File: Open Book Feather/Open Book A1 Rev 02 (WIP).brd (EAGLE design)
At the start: 77.5 x 112.3 mm, 114 parts, among them J1 SJ-43514-SMT, J2 10118193-0001LF, Q1 DMG341, Q2 IRLML0100, SW1 SPDT_SWITCH, U1 AP2112-3.3, U2 MCP73831T-2ACI/OT, U3 ATSAMD51J64-TQFP(10X10), U4 GD25Q16C (or GD25Q32C), U5 74AC165D, U6 GD25Q16C (or GD25Q32C), U7 23K256-I/SN, X1 JSTPH, X2 2x5 0.05" SWD

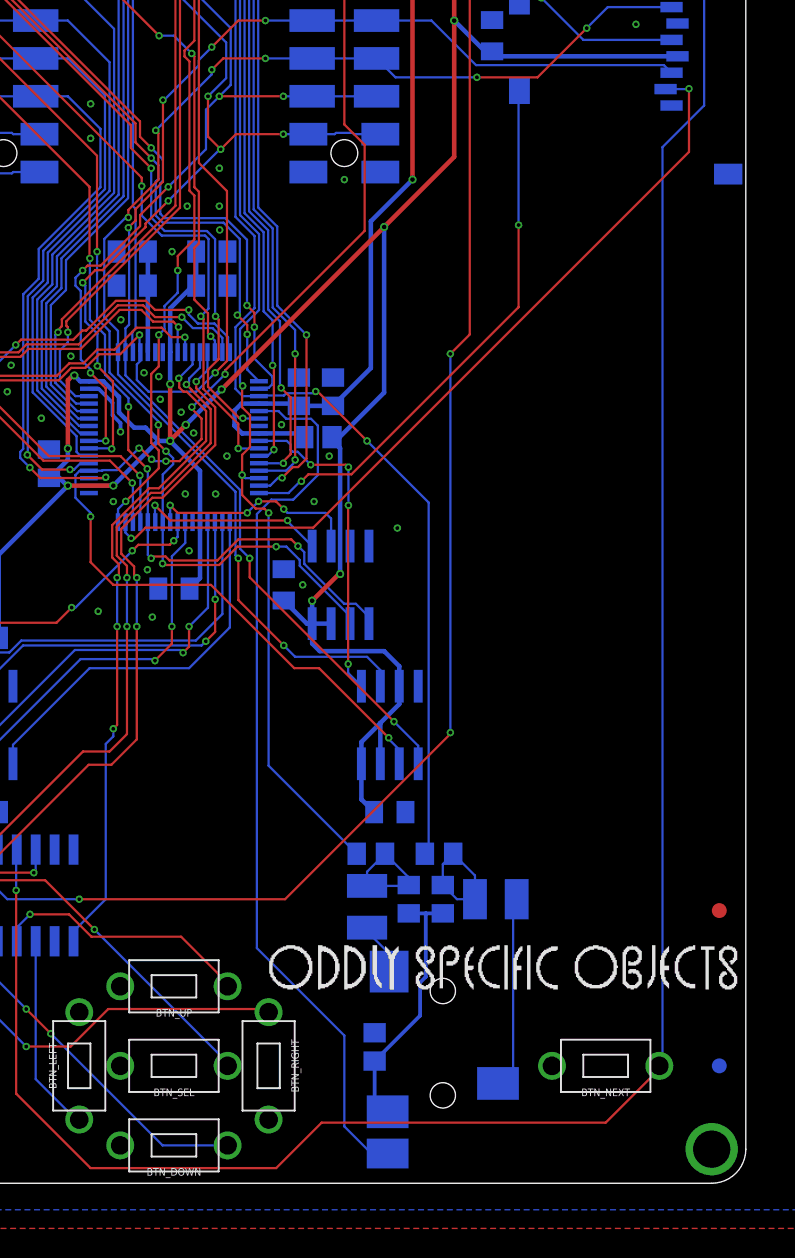
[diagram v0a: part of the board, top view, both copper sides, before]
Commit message: added mic preamp
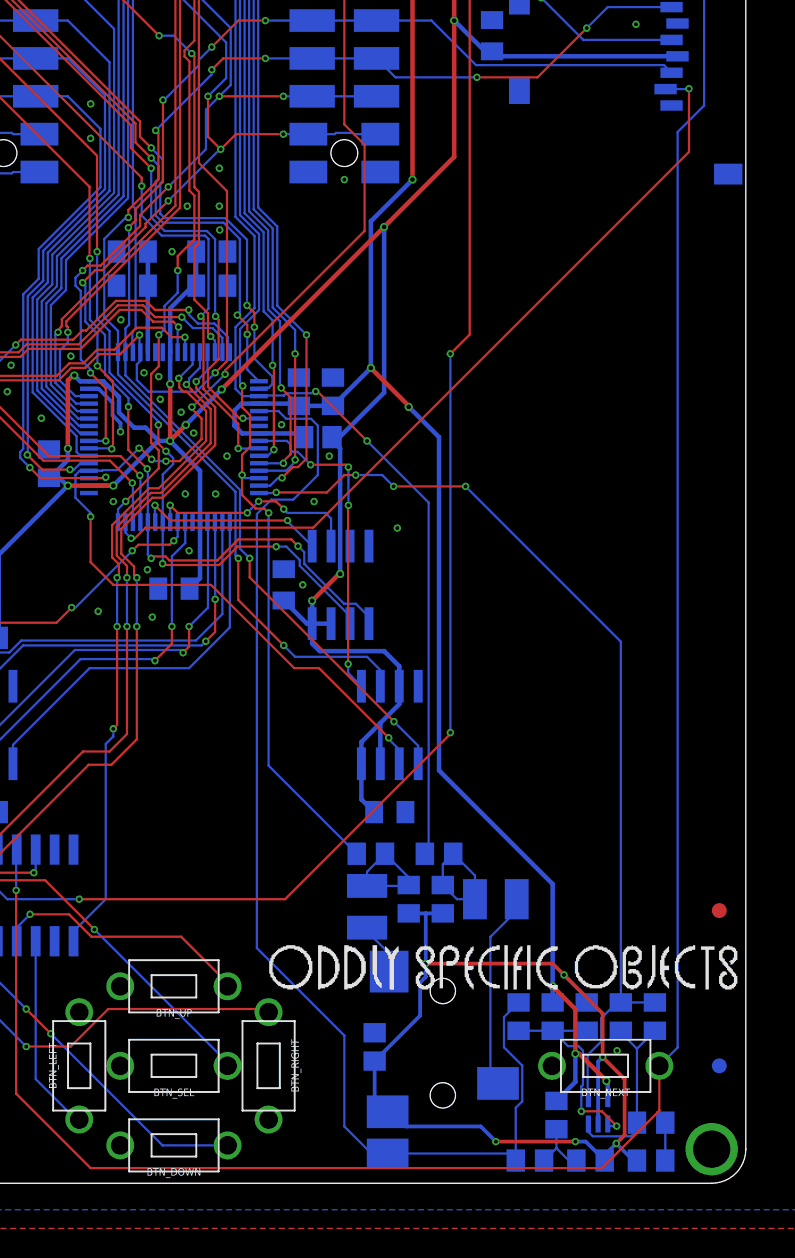
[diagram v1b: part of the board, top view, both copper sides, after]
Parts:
- added C32: 0.1µF, microbuilder:0805-NO
- added C33: 0.01uF, microbuilder:0805-NO
- added C34: 100pF, microbuilder:0805-NO
- added C35: 10uF, microbuilder:0805-NO
- added R10, R11: 1M, microbuilder:0805-NO
- added R12: 100K, microbuilder:0805-NO
- added R13, R23, R24: 1K, microbuilder:0805-NO
- added U8: MAX4466EXK+T, microbuilder:SC70-5
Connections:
- new net A10_MICAMP: C34.1, R12.2, U3.16, U8.4
- new net N$65: C32.1, R13.2, R23.1
- new net N$67: C33.2, R10.2, R11.1, U8.1
- new net N$68: C34.2, R12.1, R24.1, U8.3
- new net N$69: C35.1, R24.2
- net A7_MIC: now also C33.1, R13.1
- net AGND: now also C32.2, C35.2, R10.1, U8.2
- net AVCC: now also R11.2, R23.2, U8.5
- net SD_CD: no longer U3.16
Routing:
- net A10_MICAMP: track 0.00 -> 63.4 mm, vias 0 -> 4
- net AVCC: track 69.3 -> 129.8 mm, vias 2 -> 7
- net AGND: track 17.4 -> 66.5 mm, vias 0 -> 6
- net SD_CD: track 37.1 -> 0.00 mm, vias 2 -> 0
- net A7_MIC: track 60.0 -> 80.5 mm
- net N$67: track 0.00 -> 14.7 mm, vias 0 -> 2
- net N$68: track 0.00 -> 12.9 mm
- net N$65: track 0.00 -> 4.12 mm
- net N$69: track 0.00 -> 2.54 mm
- net BUTTON6: track 147.7 -> 149.3 mm
- net GND: vias 44 -> 45
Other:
- board text added: "+MIC PREAMP"
- board text added: "A0: Right audio out A1: Left audio out A7: Raw mic in"
- board text added: "U8 is a MAX4466 amp for an inline electret mic. A10: louder mic in."
- board text removed: "(like the old iPhone ones) you can detect button presses when A7 shorts to ground."
- board text removed: "3.5mm jack J1 does a lot! Dual DACs on A0 and A1 drive the R and L channels, respectively. If your earphones have an inline mic, you can read that signal on pin A7. And if it has a one button remote"

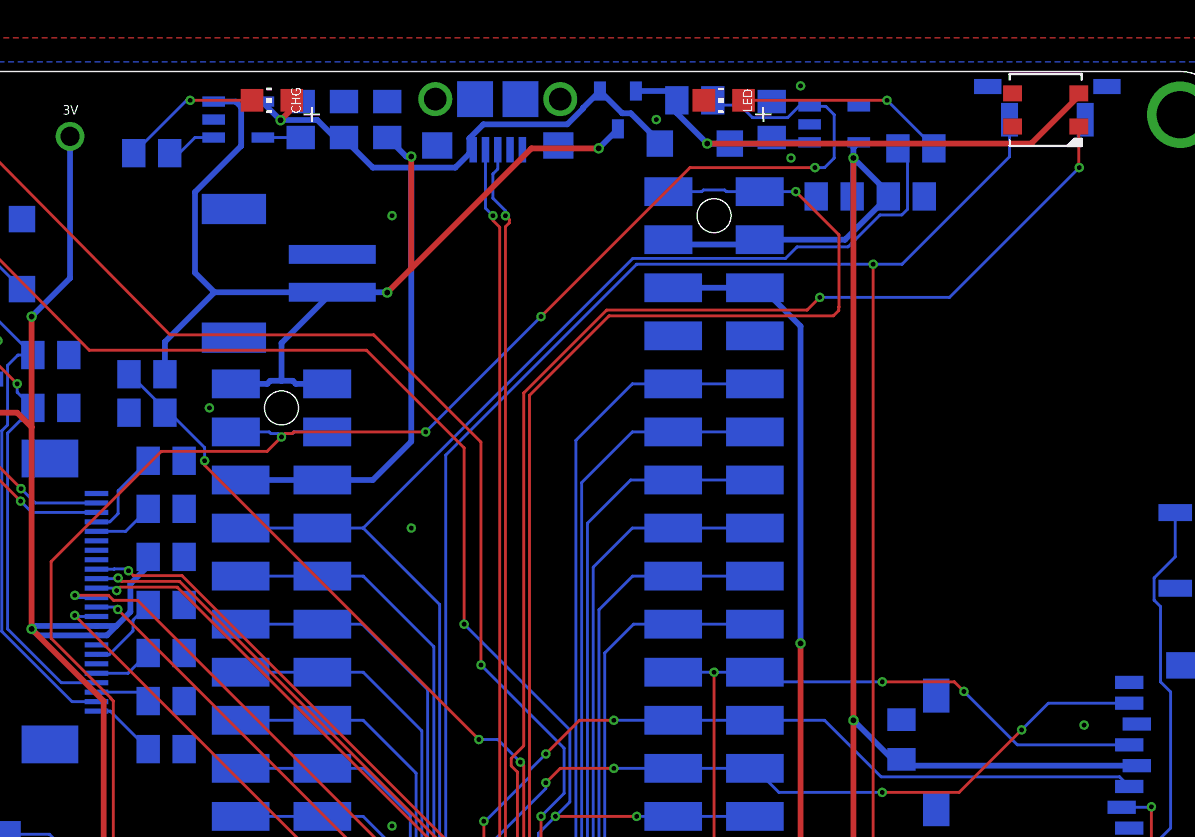
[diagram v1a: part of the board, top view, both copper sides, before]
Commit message: rearrange power supply block, power neopixel from regulator
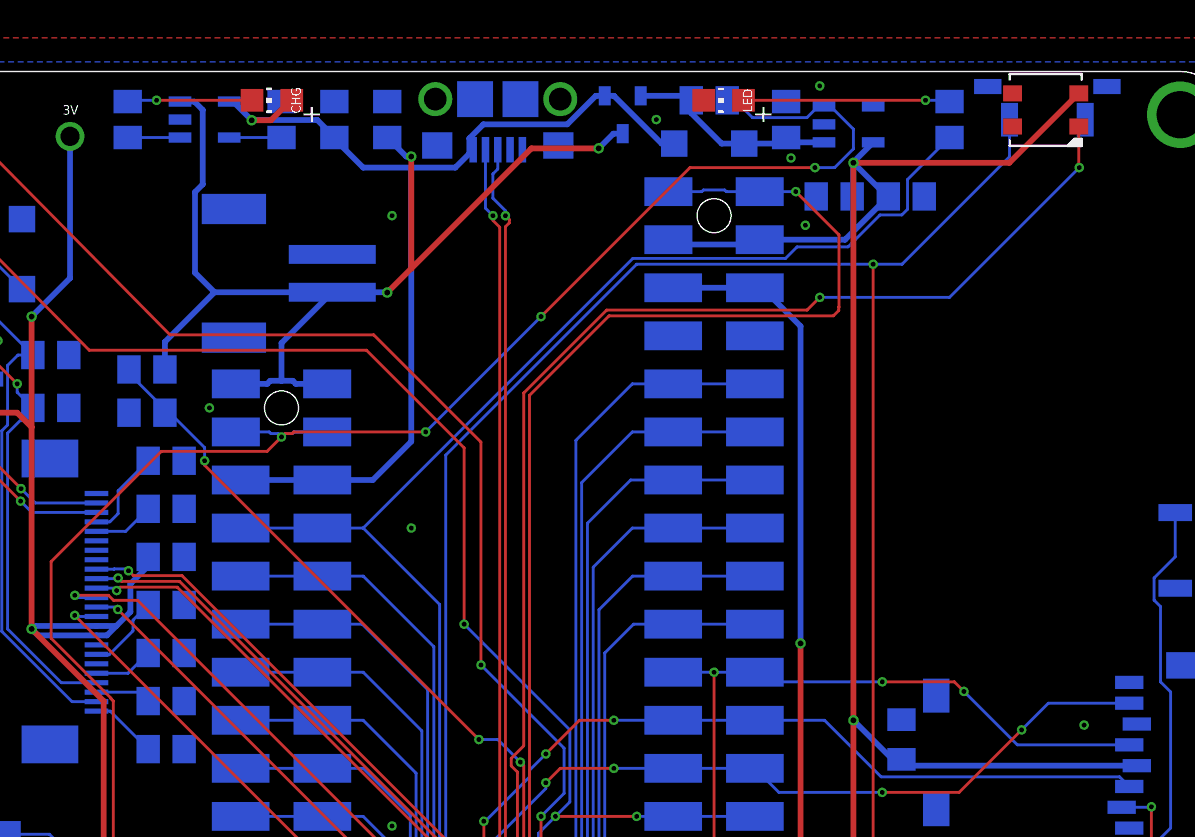
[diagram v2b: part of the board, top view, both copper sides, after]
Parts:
- moved R8 2.34 mm to (62.7, 109.7), turned to 90 degrees
- moved R4 2.18 mm to (19.3, 109.7), turned to 270 degrees
- moved U2 1.78 mm to (23.4, 109.7)
- moved R3 1.02 mm to (27.4, 109.7)
- moved U1 0.76 mm to (57.4, 109.5)
- moved C1 0.76 mm to (54.1, 109.7)
- moved D1 0.76 mm to (50.0, 108.5)
- moved R1 0.76 mm to (50.0, 110.7)
- moved R2 0.51 mm to (30.2, 109.7)
- moved Q1 0.36 mm to (45.5, 110.0)
- moved R15 0.25 mm to (20.3, 96.5)
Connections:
- net +3V3: now also STATUS.2
- net V+: no longer STATUS.2
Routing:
- net V+: track 31.8 -> 11.4 mm, vias 1 -> 0
- net +3V3: track 434.0 -> 447.3 mm
- net VBUS: track 51.8 -> 55.3 mm
- net VBAT: track 61.5 -> 60.2 mm
- net D13: track 87.3 -> 88.6 mm
- net N$4: track 7.41 -> 6.60 mm
- net PROG: track 2.00 -> 2.76 mm
- net EN: track 152.0 -> 152.6 mm
- net GND: vias 45 -> 46
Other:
- board text added: "(for red LED #13)"

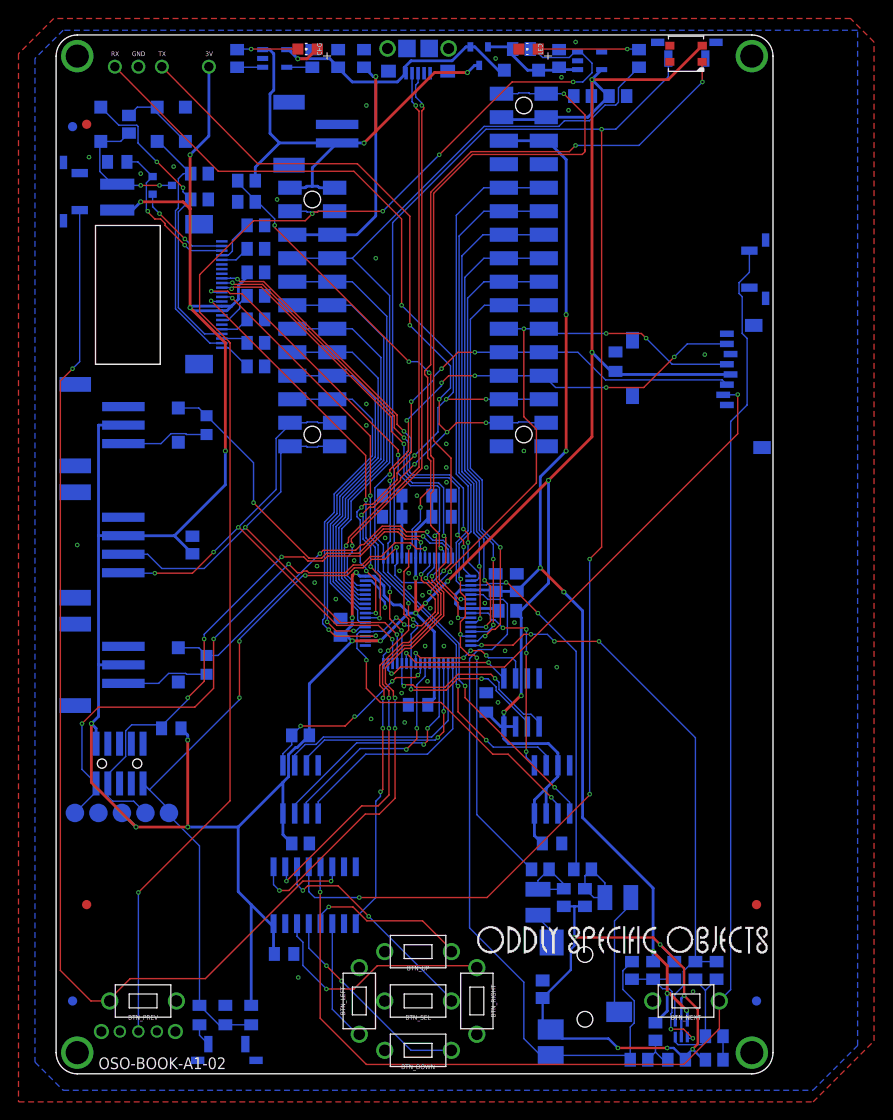
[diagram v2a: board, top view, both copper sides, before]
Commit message: fix buttons, add pulldown resistors & remove lock btn from shift reg
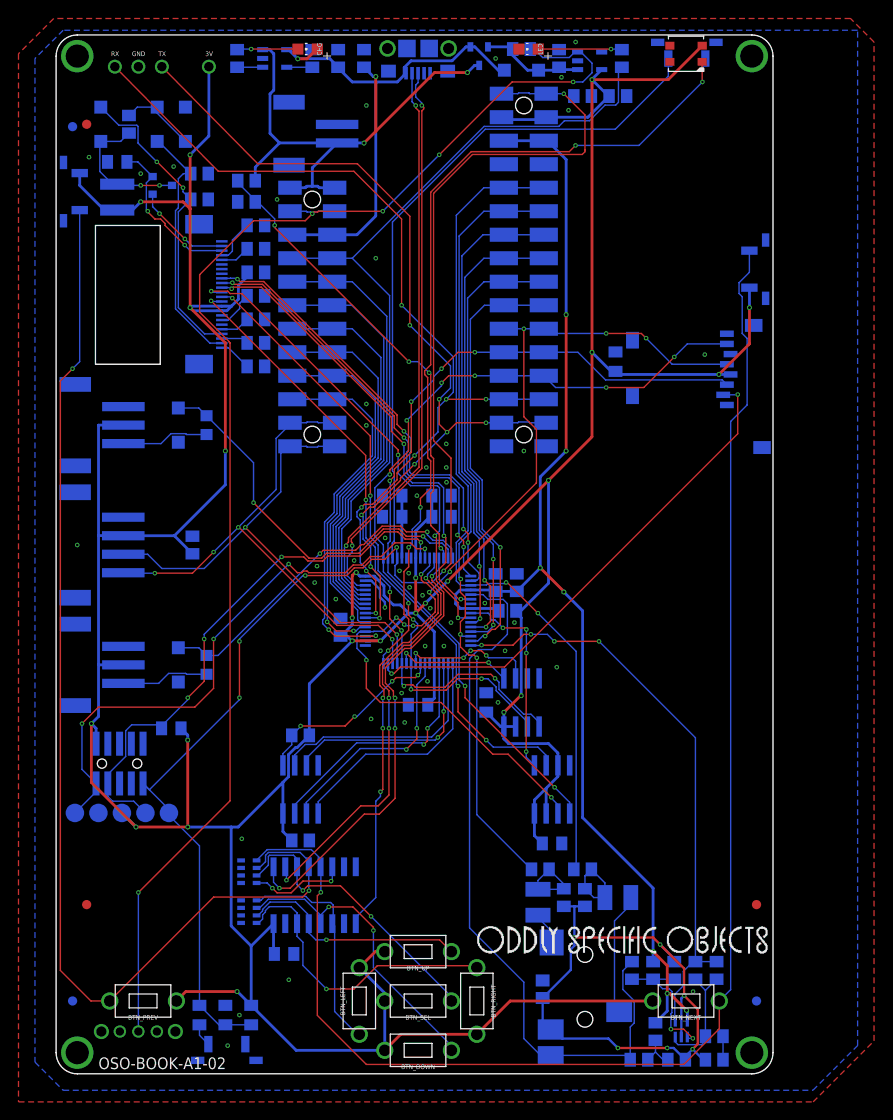
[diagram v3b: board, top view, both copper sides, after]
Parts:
- added R26, R27: 100K, resistor array:EXBV8V
- LED: value RED OR GRN -> RED
- moved R8 1.85 mm to (60.9, 109.7)
- moved C14 0.33 mm to (26.2, 25.2)
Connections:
- new net BUTTONLOCK: BTN_LOCK.P$1, U3.51
- net +3V3: now also BTN_NEXT_ALT.P$2, BTN_PREV_ALT.P$2, U$23.P$2, U$46.P$2, U$49.P$2, U$50.P$2, U$51.P$2, U$52.P$2, U$53.P$2
- net BUTTON0: now also R27.1
- net BUTTON1: now also R27.2, U$23.P$1; no longer U$49.P$1
- net BUTTON2: now also R27.3, U$49.P$1; no longer U$23.P$1
- net BUTTON3: now also R27.4
- net BUTTON4: now also R26.3
- net BUTTON5: now also BTN_PREV_ALT.P$1, R26.2, U$53.P$1; no longer BTN_LOCK.P$1, U3.51
- net BUTTON6: now also R26.1
- net BUTTON7: now also R26.4; no longer BTN_PREV_ALT.P$1, U$53.P$1
- net GND: now also R26.5, R26.6, R26.7, R26.8, R27.5, R27.6, R27.7, R27.8; no longer BTN_NEXT_ALT.P$2, BTN_PREV_ALT.P$2, U$23.P$2, U$46.P$2, U$49.P$2, U$50.P$2, U$51.P$2, U$52.P$2, U$53.P$2
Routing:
- net BUTTON7: track 120.7 -> 10.6 mm
- net +3V3: track 447.3 -> 534.8 mm, vias 21 -> 24
- net BUTTONLOCK: track 0.00 -> 74.7 mm
- net BUTTON5: track 185.1 -> 126.5 mm, vias 4 -> 2
- net BUTTON1: track 17.5 -> 32.7 mm, vias 1 -> 2
- net BUTTON0: track 13.3 -> 24.2 mm
- net BUTTON6: track 149.3 -> 158.3 mm
- net BUTTON4: track 24.4 -> 31.4 mm
- net BUTTON3: track 25.8 -> 32.7 mm
- net BUTTON2: track 22.6 -> 25.1 mm, vias 2 -> 1
- net N$7: track 10.9 -> 9.06 mm
- net D13: track 88.6 -> 87.9 mm
- net GND: vias 46 -> 49
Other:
- board text added: "Bits: 0: LEFT 1: DOWN 2: UP 3: RIGHT 4: SEL 5: PREV 6: NEXT 7:"
- board text added: "R1 up top pulls EN high. SW1 pulls EN low when switched, disabling 3V power supply U1 along with most of the board."
- board text added: "R8: current limiting for LED #13"
- board text added: "The Open Book by Joey Castillo @josecastillo. Based in large part on @Adafruit's great open source designs. OSO logo & lazer bear by Joseph Devens, @DoctorDevens. Thanks to Tom F, Josh L, Brent R & many others. Made with . in Brooklyn & Texas"
- board text removed: "(for red LED #13)"
- board text removed: "Bits: 0: LEFT 1: DOWN 2: UP 3: RIGHT 4: SEL 5: PREV 6: NEXT 7: LOCK"
- board text removed: "R1 up top pulls EN high. SW1 pulls EN low when switched, disabling 3V power supply U1& most of the board."
- board text removed: "The Open Book by Joey Castillo @josecastillo. Based in large part on @Adafruit's great open source designs. OSO Logo & lazer bear by Joseph Devens, @DoctorDevens. Thanks to Josh L, Tom F, Brent R. Thanks to 20 years of volunteers behind GNU Unifont: Unifoundry.com. Crafted with . in Brooklyn & Texas."
- board text removed: "not a PWM RGB LED! This: https://adafru.it/1938 Data pin at right, power is higher of VBAT and VBUS."

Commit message: put sd card detect signal on shift register
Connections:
- removed net SD_CD: MICROSD.CD2
- net +3V3: now also R26.5
- net BUTTON7: now also MICROSD.CD2
- net GND: no longer R26.5
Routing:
- net +3V3: track 534.8 -> 535.8 mm
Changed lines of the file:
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@@
 <grid distance="0.01" unitdist="inch" unit="inch" style="lines" multiple="1" display="no" altdistance="1" altunitdist="mil" altunit="inch"/>
 <layers>
-<layer number="1" name="Top" color="4" fill="1" visible="yes" active="yes"/>
+<layer number="1" name="Top" color="4" fill="1" visible="no" active="yes"/>
 <layer number="2" name="Route2" color="1" fill="3" visible="no" active="no"/>
 <layer number="3" name="Route3" color="4" fill="3" visible="no" active="no"/>
@@
 interface on SERCOM4.
 Chip select SRCS is D53.</text>
-<text x="72.898" y="2.286" size="2.032" layer="29" font="vector" ratio="18" distance="20" align="center-right">THE OPEN BOOK</text>
+<text x="72.898" y="2.286" size="2.032" layer="21" font="vector" ratio="18" distance="20" align="center-right">THE OPEN BOOK</text>
 <wire x1="23.114" y1="38.354" x2="23.114" y2="75.4888" width="0.1524" layer="22" style="shortdash"/>
 <wire x1="23.114" y1="75.4888" x2="0" y2="75.4888" width="0.1524" layer="22" style="shortdash"/>
@@
 <contactref element="R26" pad="7"/>
 <contactref element="R26" pad="6"/>
-<contactref element="R26" pad="5"/>
 <contactref element="R27" pad="8"/>
 <contactref element="R27" pad="7"/>
@@
 <wire x1="49.9316" y1="40.8638" x2="48.133" y2="39.0652" width="0.3048" layer="1"/>
 <via x="48.133" y="39.0652" extent="1-16" drill="0.3048"/>
-<wire x1="18.66205" y1="26.67" x2="18.66205" y2="15.98355" width="0.3048" layer="16"/>
+<wire x1="18.66205" y1="26.67" x2="18.66205" y2="20.6248" width="0.3048" layer="16"/>
+<wire x1="18.66205" y1="20.6248" x2="18.66205" y2="15.98355" width="0.3048" layer="16"/>
 <wire x1="20.828" y1="7.4" x2="20.828" y2="13.8176" width="0.3048" layer="16"/>
 <wire x1="53.975" y1="33.334" x2="53.975" y2="34.671" width="0.3048" layer="16"/>
@@
 <wire x1="64.218" y1="7.874" x2="48.812" y2="7.874" width="0.3048" layer="1"/>
 <wire x1="48.812" y1="7.874" x2="45.212" y2="4.274" width="0.3048" layer="1"/>
+<contactref element="R26" pad="5"/>
+<wire x1="19.7358" y1="20.6248" x2="18.66205" y2="20.6248" width="0.3048" layer="16"/>
 </signal>
 <signal name="GDR">
@@
 <contactref element="MS1" pad="7'"/>
 </signal>
-<signal name="SD_CD">
-<contactref element="MICROSD" pad="CD2"/>
-</signal>
 <signal name="+3V1">
 </signal>
@@
 <wire x1="23.622" y1="19.558" x2="23.114" y2="20.066" width="0.1524" layer="1"/>
 <wire x1="29.464" y1="20.828" x2="26.416" y2="20.828" width="0.1524" layer="1"/>
+<contactref element="MICROSD" pad="CD2"/>
+<wire x1="29.591" y1="22.3774" x2="62.035" y2="73.28" width="0" layer="19" extent="16-16"/>
 </signal>
 <signal name="A7_MIC">
